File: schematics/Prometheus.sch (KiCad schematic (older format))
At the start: 12 parts, among them J1 ATX Power Conn, SW1 Reset Switch, SW2 Power Switch, U1 wdc65c816, U2 DS1501YN, X1 14MHz, X2 32kHz

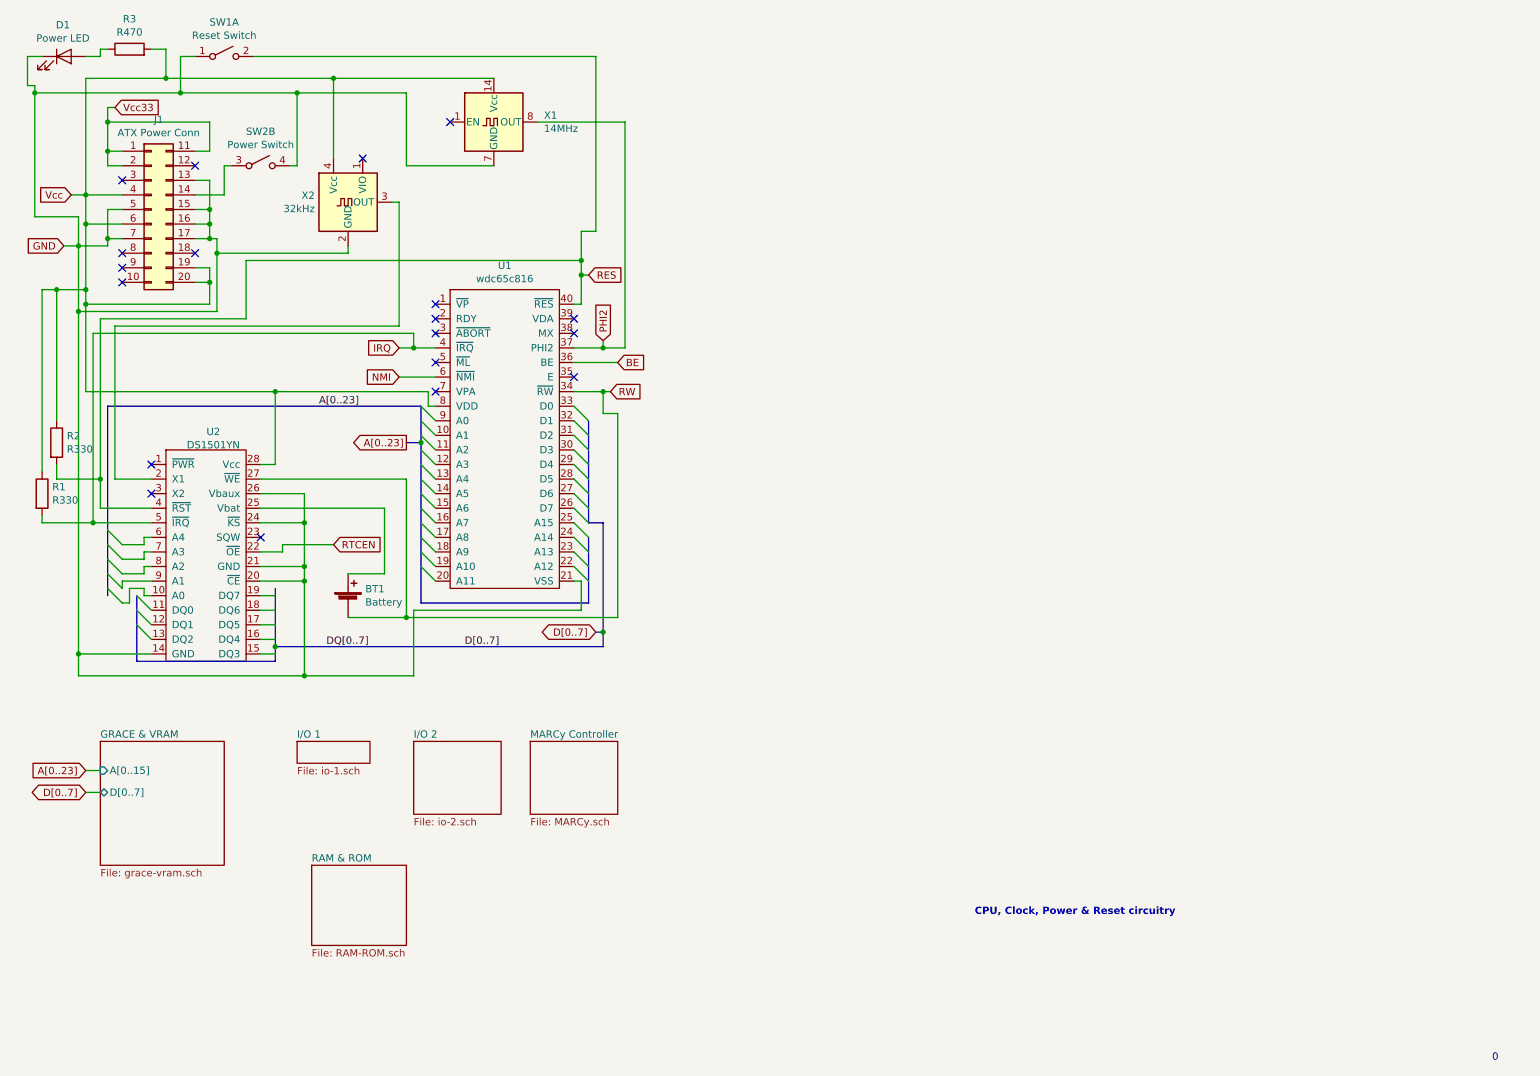
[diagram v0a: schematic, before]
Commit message: Cleanup and spot check for main sheet
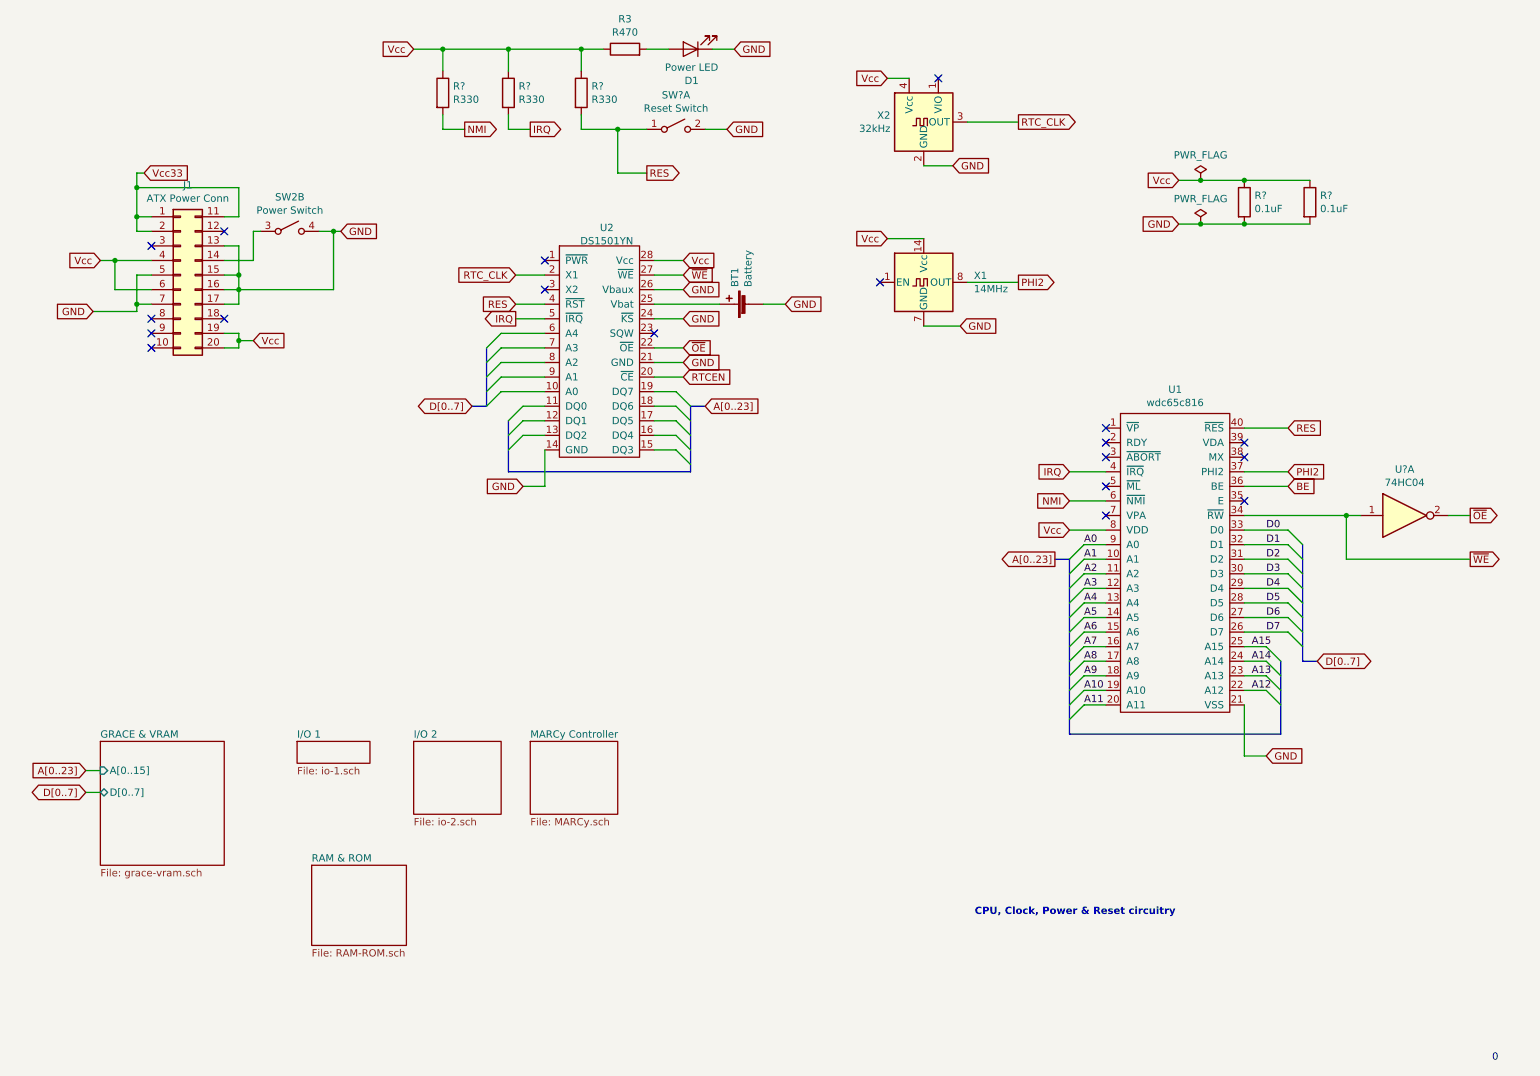
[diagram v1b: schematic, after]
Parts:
- removed R1, R2: R330, symbol Device:R
- removed SW1: Reset Switch, symbol Switch:SW_DPST_x2
- added R? (x3): R330, symbol Device:R
- added R? (x2): 0.1uF, symbol Device:R
- added SW?: Reset Switch, symbol Switch:SW_DPST_x2
- added U?: 74HC04, symbol 74xx:74HC04
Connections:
- net labels added: A0, A1, A10, A11, A12, A13, A14, A15, A2, A3, A4, A5, A6, A7, A8, A9, D0, D1, D2, D3, D4, D5, D6, D7, RTC_CLK, ~OE, ~WE
- net labels removed: DQ[0..7], RW
- wire segments 171 -> 134
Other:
- moved on the sheet: BT1, D1, J1, R3, SW2B, U1, U2, X1, X2

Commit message: merge from Jani's commit
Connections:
- net A0: now also U2.10 (A0)
- net A1: now also U2.9 (A1)
- net A2: now also U2.8 (A2)
- net A3: now also U2.7 (A3)
- net A4: now also U2.6 (A4)
- net D0: now also U2.11 (DQ0)
- net D1: now also U2.12 (DQ1)
- net D2: now also U2.13 (DQ2)
- net D3: now also U2.15 (DQ3)
- net D4: now also U2.16 (DQ4)
- net D5: now also U2.17 (DQ5)
- net D6: now also U2.18 (DQ6)
- net D7: now also U2.19 (DQ7)
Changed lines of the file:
@@
 $EndSheet
 $Sheet
-S 2400 5450 500  150
+S 2350 5450 650  600
 U 5F475375
 F0 "I/O 1" 50
@@
 Wire Bus Line
 	3700 3150 3600 3150
-Text GLabel 5200 3150 2    50   Input ~ 0
+Text GLabel 3600 3150 0    50   Input ~ 0
 A[0..23]
-Text GLabel 3600 3150 0    50   BiDi ~ 0
+Text GLabel 5200 3150 2    50   BiDi ~ 0
 D[0..7]
 Wire Wire Line
@@
 Wire Wire Line
 	2000 2700 2000 2750
+Text Label 3950 3150 0    50   ~ 0
+D0
+Text Label 3950 3250 0    50   ~ 0
+D1
+Text Label 3950 3350 0    50   ~ 0
+D2
+Text Label 3950 2650 0    50   ~ 0
+A4
+Text Label 3950 2750 0    50   ~ 0
+A3
+Text Label 3950 2850 0    50   ~ 0
+A2
+Text Label 3950 2950 0    50   ~ 0
+A1
+Text Label 3950 3050 0    50   ~ 0
+A0
+Text Label 4900 3450 0    50   ~ 0
+D3
+Text Label 4900 3350 0    50   ~ 0
+D4
+Text Label 4900 3250 0    50   ~ 0
+D5
+Text Label 4900 3150 0    50   ~ 0
+D6
+Text Label 4900 3050 0    50   ~ 0
+D7
 Wire Bus Line
 	3850 3250 3850 3600

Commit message: add audio schematic, other fixes
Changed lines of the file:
@@
 $Descr A4 11693 8268
 encoding utf-8
-Sheet 1 6
+Sheet 1 7
 Title ""
 Date ""
@@
 Text Label 4900 3050 0    50   ~ 0
 D7
+$Sheet
+S 3600 6300 700  550
+U 5F16299B
+F0 "Audio" 50
+F1 "audio.sch" 50
+$EndSheet
 Wire Bus Line
 	3850 3250 3850 3600

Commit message: Minor tweaks to labels and values.
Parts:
- X1: value 14MHz -> 8MHz
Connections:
- net ~WE renamed RW
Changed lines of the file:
@@
 P 6700 2300
 F 0 "X1" H 7044 2346 50  0000 L CNN
-F 1 "14MHz" H 7044 2255 50  0000 L CNN
+F 1 "8MHz" H 7044 2255 50  0000 L CNN
 F 2 "Oscillator:Oscillator_DIP-14" H 7150 1950 50  0001 C CNN
 F 3 "http://cdn-reichelt.de/documents/datenblatt/B400/OSZI.pdf" H 6600 2300 50  0001 C CNN
@@
 F1 "audio.sch" 50
 $EndSheet
+Text GLabel 9900 3250 2    50   Input ~ 0
+RW
+Wire Wire Line
+	9900 3250 9600 3250
+Wire Wire Line
+	9600 3250 9600 3900
 Wire Bus Line
 	3850 3250 3850 3600

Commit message: connect up I/O sheet 2
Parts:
- removed R? (x2): 0.1uF, symbol Device:R
- removed U?: 74HC04, symbol 74xx:74HC04
- added C? (x2): 0.1uF, symbol Device:C
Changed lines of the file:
@@
 $EndSheet
 $Sheet
-S 3200 5450 600  500
+S 5100 4400 1050 1700
 U 5F47C633
 F0 "I/O 2" 50
 F1 "io-2.sch" 50
+F2 "A[0..23]" I L 5100 4550 50
+F3 "D[0..7]" B L 5100 4700 50
+F4 "IRQ" O L 5100 4850 50
+F5 "FDC_EN" I L 5100 5100 50
+F6 "R~W" I L 5100 5250 50
+F7 "Vcc" I R 6150 4700 50
+F8 "GND" I R 6150 4550 50
+F9 "IOR" I L 5100 5400 50
+F10 "IOW" I L 5100 5550 50
+F11 "RESET" I L 5100 5700 50
+F12 "IDE_LDR" I R 6150 4950 50
+F13 "IDE_LDW" I R 6150 5200 50
+F14 "IDE_UDR" I R 6150 5050 50
+F15 "IDE_UDW" I R 6150 5300 50
+F16 "IRQ_HIGH" O L 5100 4950 50
 $EndSheet
 $Sheet
-S 4000 5450 600  500
+S 1150 6850 600  500
 U 5F47CC44
 F0 "MARCy Controller" 50
@@
 NoConn ~ 7950 3700
 NoConn ~ 7950 3300
-Text GLabel 10450 4200 2    50   Output ~ 0
-~WE
 Wire Wire Line
 	8900 4000 9200 4000
@@
 $EndComp
 Wire Wire Line
-	9350 1900 8900 1900
-Connection ~ 8900 1600
-Wire Wire Line
-	8900 1600 9350 1600
-$Comp
-L Device:R R?
-U 1 1 5F5C22AE
-P 9350 1750
-F 0 "R?" H 9420 1796 50  0000 L CNN
-F 1 "0.1uF" H 9420 1705 50  0000 L CNN
-F 2 "" V 9280 1750 50  0001 C CNN
-F 3 "~" H 9350 1750 50  0001 C CNN
-	1    9350 1750
-	1    0    0    -1
-$EndComp
-$Comp
-L Device:R R?
-U 1 1 5F5C1E3A
-P 8900 1750
-F 0 "R?" H 8970 1796 50  0000 L CNN
-F 1 "0.1uF" H 8970 1705 50  0000 L CNN
-F 2 "" V 8830 1750 50  0001 C CNN
-F 3 "~" H 8900 1750 50  0001 C CNN
-	1    8900 1750
-	1    0    0    -1
-$EndComp
-Wire Wire Line
 	8450 1600 8600 1600
 Connection ~ 8600 1600
-Wire Wire Line
-	8600 1600 8900 1600
-Wire Wire Line
-	8600 1900 8900 1900
 Connection ~ 8600 1900
-Connection ~ 8900 1900
 Text GLabel 8450 1900 0    50   Input ~ 0
 GND
@@
 Wire Wire Line
 	4850 2950 5050 2950
-$Comp
-L 74xx:74HC04 U?
-U 1 1 5F89027D
-P 10000 3900
-F 0 "U?" H 10000 4217 50  0000 C CNN
-F 1 "74HC04" H 10000 4126 50  0000 C CNN
-F 2 "" H 10000 3900 50  0001 C CNN
-F 3 "https://assets.nexperia.com/documents/data-sheet/74HC_HCT04.pdf" H 10000 3900 50  0001 C CNN
-	1    10000 3900
-	1    0    0    -1
-$EndComp
-Text GLabel 10450 3900 2    50   Output ~ 0
-~OE
-Wire Wire Line
-	8900 3900 9600 3900
-Wire Wire Line
-	10450 3900 10300 3900
-Wire Wire Line
-	10450 4200 9600 4200
-Wire Wire Line
-	9600 4200 9600 3900
-Connection ~ 9600 3900
-Wire Wire Line
-	9600 3900 9700 3900
 Text GLabel 5050 2750 2    50   Input ~ 0
 ~OE
@@
 F1 "audio.sch" 50
 $EndSheet
-Text GLabel 9900 3250 2    50   Input ~ 0
+Text GLabel 9200 3900 2    50   Output ~ 0
 RW
 Wire Wire Line
-	9900 3250 9600 3250
-Wire Wire Line
-	9600 3250 9600 3900
+	9200 3900 8900 3900
+Wire Wire Line
+	8600 1600 8950 1600
+Wire Wire Line
+	8600 1900 8950 1900
+$Comp
+L Device:C C?
+U 1 1 5F54B18B
+P 9450 1750
+F 0 "C?" H 9565 1796 50  0000 L CNN
+F 1 "0.1uF" H 9565 1705 50  0000 L CNN
+F 2 "" H 9488 1600 50  0001 C CNN
+F 3 "~" H 9450 1750 50  0001 C CNN
+	1    9450 1750
+	1    0    0    -1
+$EndComp
+$Comp
+L Device:C C?
+U 1 1 5F54B236
+P 8950 1750
+F 0 "C?" H 9065 1796 50  0000 L CNN
+F 1 "0.1uF" H 9065 1705 50  0000 L CNN
+F 2 "" H 8988 1600 50  0001 C CNN
+F 3 "~" H 8950 1750 50  0001 C CNN
+	1    8950 1750
+	1    0    0    -1
+$EndComp
+Wire Wire Line
+	8950 1600 9450 1600
+Connection ~ 8950 1600
+Wire Wire Line
+	8950 1900 9450 1900
+Connection ~ 8950 1900
+Text GLabel 6250 4550 2    50   Input ~ 0
+GND
+Text GLabel 6250 4700 2    50   Input ~ 0
+Vcc
+Text GLabel 5000 4550 0    50   Output ~ 0
+A[0..23]
+Text GLabel 5000 4850 0    50   Input ~ 0
+IRQ
+Text GLabel 5000 5250 0    50   Output ~ 0
+RW
+Text GLabel 5000 5700 0    50   Input ~ 0
+RES
+Wire Wire Line
+	5000 5700 5100 5700
+Wire Wire Line
+	5000 5250 5100 5250
+Wire Wire Line
+	5000 4850 5100 4850
+Wire Wire Line
+	5000 4550 5100 4550
+Wire Wire Line
+	6150 4550 6250 4550
+Wire Wire Line
+	6150 4700 6250 4700
 Wire Bus Line
 	3850 3250 3850 3600

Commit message: rename A[0..23] to A[0..15]
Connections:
- net labels added: A[0..15]
- net labels removed: A[0..23]
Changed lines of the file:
@@
 	2100 2150 1900 2150
 Text GLabel 950  5650 0    50   Input ~ 0
-A[0..23]
+A[0..15]
 Wire Wire Line
 	1050 5650 950  5650
@@
 $EndSheet
 $Sheet
-S 2350 5450 650  600
+S 850  3600 650  600
 U 5F475375
 F0 "I/O 1" 50
@@
 F0 "I/O 2" 50
 F1 "io-2.sch" 50
-F2 "A[0..23]" I L 5100 4550 50
-F3 "D[0..7]" B L 5100 4700 50
-F4 "IRQ" O L 5100 4850 50
-F5 "FDC_EN" I L 5100 5100 50
-F6 "R~W" I L 5100 5250 50
-F7 "Vcc" I R 6150 4700 50
-F8 "GND" I R 6150 4550 50
-F9 "IOR" I L 5100 5400 50
-F10 "IOW" I L 5100 5550 50
-F11 "RESET" I L 5100 5700 50
-F12 "IDE_LDR" I R 6150 4950 50
-F13 "IDE_LDW" I R 6150 5200 50
-F14 "IDE_UDR" I R 6150 5050 50
-F15 "IDE_UDW" I R 6150 5300 50
-F16 "IRQ_HIGH" O L 5100 4950 50
+F2 "D[0..7]" B L 5100 4700 50
+F3 "IRQ" O L 5100 4850 50
+F4 "FDC_EN" I L 5100 5100 50
+F5 "R~W" I L 5100 5250 50
+F6 "Vcc" I R 6150 4700 50
+F7 "GND" I R 6150 4550 50
+F8 "IOR" I L 5100 5400 50
+F9 "IOW" I L 5100 5550 50
+F10 "RESET" I L 5100 5700 50
+F11 "IDE_LDR" I R 6150 4950 50
+F12 "IDE_LDW" I R 6150 5200 50
+F13 "IDE_UDR" I R 6150 5050 50
+F14 "IDE_UDW" I R 6150 5300 50
+F15 "IRQ_HIGH" O L 5100 4950 50
+F16 "A[0..15]" I L 5100 4550 50
 $EndSheet
 $Sheet
@@
 $EndSheet
 $Sheet
-S 2500 6300 650  550
+S 3250 4400 650  550
 U 5F47D036
 F0 "RAM & ROM" 50
@@
 $EndComp
 Text GLabel 7600 4200 0    50   Output ~ 0
-A[0..23]
+A[0..15]
 Text GLabel 9200 3600 2    50   Input ~ 0
 PHI2
@@
 	3700 3150 3600 3150
 Text GLabel 3600 3150 0    50   Input ~ 0
-A[0..23]
+A[0..15]
 Text GLabel 5200 3150 2    50   BiDi ~ 0
 D[0..7]
@@
 D7
 $Sheet
-S 3600 6300 700  550
+S 5550 6700 700  550
 U 5F16299B
 F0 "Audio" 50
@@
 Vcc
 Text GLabel 5000 4550 0    50   Output ~ 0
-A[0..23]
+A[0..15]
 Text GLabel 5000 4850 0    50   Input ~ 0
 IRQ

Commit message: begin wiring up the hierarchial sheets
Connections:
- net labels added: CAS, FDC_EN, IDE_CS0, IDE_CS1, IDE_LDR, IDE_LDW, IDE_UDR, IDE_UDW, IOR, IOW, MA[0..11], RAS, ROM_EN
- wire segments 136 -> 184
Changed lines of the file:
@@
 Wire Wire Line
 	2100 2150 1900 2150
-Text GLabel 950  5650 0    50   Input ~ 0
+Text GLabel 1850 3200 0    50   Input ~ 0
 A[0..15]
 Wire Wire Line
-	1050 5650 950  5650
-Text GLabel 950  5800 0    50   BiDi ~ 0
+	1950 3200 1850 3200
+Text GLabel 1850 3350 0    50   BiDi ~ 0
 D[0..7]
 Wire Wire Line
-	1050 5800 950  5800
+	1950 3350 1850 3350
 $Sheet
-S 1050 5450 850  850
+S 1950 3000 850  850
 U 5EF72E92
 F0 "GRACE & VRAM" 50
 F1 "grace-vram.sch" 50
-F2 "A[0..15]" I L 1050 5650 50
-F3 "D[0..7]" B L 1050 5800 50
+F2 "A[0..15]" I L 1950 3200 50
+F3 "D[0..7]" B L 1950 3350 50
 $EndSheet
 $Sheet
@@
 $EndSheet
 $Sheet
-S 5100 4400 1050 1700
+S 5100 4400 1050 1400
 U 5F47C633
 F0 "I/O 2" 50
@@
 F15 "IRQ_HIGH" O L 5100 4950 50
 F16 "A[0..15]" I L 5100 4550 50
+F17 "IDE_CS0" I R 6150 5500 50
+F18 "IDE_CS1" I R 6150 5600 50
 $EndSheet
 $Sheet
-S 1150 6850 600  500
+S 1200 4650 950  2550
 U 5F47CC44
 F0 "MARCy Controller" 50
 F1 "MARCy.sch" 50
-$EndSheet
-$Sheet
-S 3250 4400 650  550
-U 5F47D036
-F0 "RAM & ROM" 50
-F1 "RAM-ROM.sch" 50
+F2 "MA[0..11]" O R 2150 5100 50
+F3 "A[0..15]" I L 1200 4900 50
+F4 "R~W" I L 1200 5250 50
+F5 "~OE" O R 2150 5400 50
+F6 "RTC_EN" O R 2150 5750 50
+F7 "VIA1_EN" O R 2150 5850 50
+F8 "VIA2_EN" O R 2150 5950 50
+F9 "ROM_EN" O R 2150 6050 50
+F10 "RAM_EN" O R 2150 6150 50
+F11 "UART_EN" O R 2150 6250 50
+F12 "GRACE_EN" O R 2150 6350 50
+F13 "AUDIO_EN" O R 2150 6450 50
+F14 "FDC_EN" O R 2150 6550 50
+F15 "CAS" O L 1200 5950 50
+F16 "RAS" O L 1200 6050 50
+F17 "IDE_EN" O R 2150 6650 50
+F18 "IOW" O L 1200 6300 50
+F19 "IOR" O L 1200 6400 50
+F20 "IDE_CS1" O L 1200 6600 50
+F21 "IDE_CS0" O L 1200 6500 50
+F22 "IDE_UDW" O L 1200 6800 50
+F23 "IDE_LDW" O L 1200 6700 50
+F24 "IDE_UDR" O L 1200 7000 50
+F25 "IDE_LDR" O L 1200 6900 50
+F26 "GND" I R 2150 4750 50
+F27 "Vcc33" I R 2150 4850 50
+F28 "PHI2" I L 1200 5100 50
 $EndSheet
 Text GLabel 1350 1550 2    50   Input ~ 0
@@
 D7
 $Sheet
-S 5550 6700 700  550
+S 6100 3600 700  550
 U 5F16299B
 F0 "Audio" 50
@@
 Text GLabel 6250 4700 2    50   Input ~ 0
 Vcc
-Text GLabel 5000 4550 0    50   Output ~ 0
+Text GLabel 5000 4550 0    50   Input ~ 0
 A[0..15]
-Text GLabel 5000 4850 0    50   Input ~ 0
+Text GLabel 5000 4850 0    50   Output ~ 0
 IRQ
-Text GLabel 5000 5250 0    50   Output ~ 0
+Text GLabel 5000 5250 0    50   Input ~ 0
 RW
 Text GLabel 5000 5700 0    50   Input ~ 0
@@
 Wire Wire Line
 	6150 4700 6250 4700
+$Sheet
+S 5200 6600 850  800
+U 5F47D036
+F0 "RAM & ROM" 50
+F1 "RAM-ROM.sch" 50
+F2 "D[0..7]" B L 5200 6850 50
+F3 "A[0..15]" I L 5200 6750 50
+F4 "VCC" I R 6050 6800 50
+F5 "GND" I R 6050 6700 50
+F6 "DQ[0..7]" B L 5200 7000 50
+F7 "MA[0..11]" I L 5200 7150 50
+F8 "CAS" I R 6050 6950 50
+F9 "RAS" I R 6050 7050 50
+F10 "R~W" I L 5200 7300 50
+F11 "ROM_EN" I R 6050 7250 50
+$EndSheet
+Wire Wire Line
+	6050 6700 6150 6700
+Wire Wire Line
+	6050 6800 6150 6800
+Text GLabel 6150 6700 2    50   Input ~ 0
+GND
+Text GLabel 6150 6800 2    50   Input ~ 0
+Vcc
+Wire Wire Line
+	5200 6750 5100 6750
+Wire Wire Line
+	5200 6850 5100 6850
+Wire Wire Line
+	5200 7000 5100 7000
+Wire Wire Line
+	5200 7150 5100 7150
+Text GLabel 5100 6750 0    50   Input ~ 0
+A[0..15]
+Wire Wire Line
+	5100 4700 5000 4700
+Text GLabel 5000 4700 0    50   BiDi ~ 0
+D[0..7]
+Text GLabel 5100 6850 0    50   BiDi ~ 0
+D[0..7]
+Wire Wire Line
+	1200 4900 1100 4900
+Wire Wire Line
+	1200 5100 1100 5100
+Wire Wire Line
+	1200 5250 1100 5250
+Wire Wire Line
+	1200 5950 1100 5950
+Wire Wire Line
+	1200 6050 1100 6050
+Wire Wire Line
+	1200 6300 1100 6300
+Wire Wire Line
+	1200 6400 1100 6400
+Wire Wire Line
+	1200 6500 1100 6500
+Wire Wire Line
+	1200 6600 1100 6600
+Wire Wire Line
+	1200 6700 1100 6700
+Wire Wire Line
+	1200 6800 1100 6800
+Wire Wire Line
+	1200 6900 1100 6900
+Wire Wire Line
+	1200 7000 1100 7000
+Wire Wire Line
+	2150 4750 2250 4750
+Wire Wire Line
+	2150 4850 2250 4850
+Wire Wire Line
+	2150 5100 2250 5100
+Wire Wire Line
+	2150 5400 2250 5400
+Wire Wire Line
+	2150 5750 2250 5750
+Wire Wire Line
+	2150 5850 2250 5850
+Wire Wire Line
+	2150 5950 2250 5950
+Wire Wire Line
+	2150 6050 2250 6050
+Wire Wire Line
+	2150 6150 2250 6150
+Wire Wire Line
+	2150 6250 2250 6250
+Wire Wire Line
+	2150 6350 2250 6350
+Wire Wire Line
+	2150 6450 2250 6450
+Wire Wire Line
+	2150 6550 2250 6550
+Wire Wire Line
+	2150 6650 2250 6650
+Text GLabel 2250 4750 2    50   Input ~ 0
+GND
+Text GLabel 2250 4850 2    50   Input ~ 0
+Vcc33
+Text GLabel 2250 5100 2    50   Output ~ 0
+MA[0..11]
+Text GLabel 5100 7150 0    50   Input ~ 0
+MA[0..11]
+Text GLabel 1100 4900 0    50   Input ~ 0
+A[0..15]
+Text GLabel 1100 5100 0    50   Input ~ 0
+PHI2
+Wire Wire Line
+	5100 5400 5000 5400
+Wire Wire Line
+	5100 5550 5000 5550
+Text GLabel 5000 5400 0    50   Input ~ 0
+IOR
+Text GLabel 5000 5550 0    50   Input ~ 0
+IOW
+Text GLabel 1100 6400 0    50   Output ~ 0
+IOR
+Text GLabel 1100 6300 0    50   Output ~ 0
+IOW
+Text GLabel 2250 6550 2    50   Output ~ 0
+FDC_EN
+Text GLabel 4950 5100 0    50   Input ~ 0
+FDC_EN
+Wire Wire Line
+	4950 5100 5100 5100
+Wire Wire Line
+	5100 4950 5000 4950
+Wire Wire Line
+	6150 4950 6250 4950
+Wire Wire Line
+	6150 5050 6250 5050
+Wire Wire Line
+	6150 5200 6250 5200
+Wire Wire Line
+	6150 5300 6250 5300
+Text GLabel 6250 4950 2    50   Input ~ 0
+IDE_LDR
+Text GLabel 6250 5050 2    50   Input ~ 0
+IDE_UDR
+Text GLabel 6250 5200 2    50   Input ~ 0
+IDE_LDW
+Text GLabel 6250 5300 2    50   Input ~ 0
+IDE_UDW
+Text GLabel 1100 6900 0    50   Output ~ 0
+IDE_LDR
+Text GLabel 1100 7000 0    50   Output ~ 0
+IDE_UDR
+Text GLabel 1100 6700 0    50   Output ~ 0
+IDE_LDW
+Text GLabel 1100 6800 0    50   Output ~ 0
+IDE_UDW
+Text GLabel 2250 5400 2    50   Output ~ 0
+~OE
+Text GLabel 1100 5250 0    50   Input ~ 0
+RW
+Wire Wire Line
+	6050 6950 6150 6950
+Wire Wire Line
+	6050 7050 6150 7050
+Wire Wire Line
+	6050 7250 6150 7250
+Wire Wire Line
+	5200 7300 5100 7300
+Text GLabel 5100 7300 0    50   Input ~ 0
+RW
+Text GLabel 1100 5950 0    50   Output ~ 0
+RAS
+Text GLabel 1100 6050 0    50   Output ~ 0
+CAS
+Text GLabel 6150 7050 2    50   Input ~ 0
+RAS
+Text GLabel 6150 6950 2    50   Input ~ 0
+CAS
+Text GLabel 2250 6050 2    50   Output ~ 0
+ROM_EN
+Text GLabel 6150 7250 2    50   Input ~ 0
+ROM_EN
+Wire Wire Line
+	6150 5500 6250 5500
+Wire Wire Line
+	6150 5600 6250 5600
+Text GLabel 1100 6500 0    50   Output ~ 0
+IDE_CS0
+Text GLabel 1100 6600 0    50   Output ~ 0
+IDE_CS1
+Text GLabel 6250 5500 2    50   Input ~ 0
+IDE_CS0
+Text GLabel 6250 5600 2    50   Input ~ 0
+IDE_CS1
 Wire Bus Line
 	3850 3250 3850 3600
